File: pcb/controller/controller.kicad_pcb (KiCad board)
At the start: 4 copper layers, 80 x 100 mm, 195 parts, among them J1001 mounting-hole-grounded, J1002 mounting-hole-grounded, J1003 mounting-hole-grounded, J1004 mounting-hole-grounded, J2001 Conn_01x02_Female, J3001 Conn_01x06_Male, J3002 Conn_01x04_Male, J5001 Conn_01x02_Female, J5002 Conn_01x02_Female, J6001 RJ45, J6002 Conn_01x02_Female, J6003 Conn_01x02_Female, J7001 Conn_Coaxial, J7002 Conn_Coaxial, U2001 LMZ14201, U2002 TPS82084, U2003 TPS735, U2004 TPS735, U3001 XC7S25-L1FTGB196, U3002 S25FL127SABN, U3003 74AVC4TD245BQ, U5001 IXDD609D2, U5002 IXDD609D2, U5003 74LVC8T245, U5004 IXDD609D2, U5005 IXDD609D2, U6001 AFBR-1624Z, U6002 AFBR-2624Z, U6003 RFM-0505S, U6004 ISO3086DWR, U6005 ISO7720QDQ1, U6006 ULN2003F12, U7001 MCP6561-OT, U7002 TLV3501AIDBVR, U7003 THS4551RGT, U7004 SG3225, U7005 AD9609

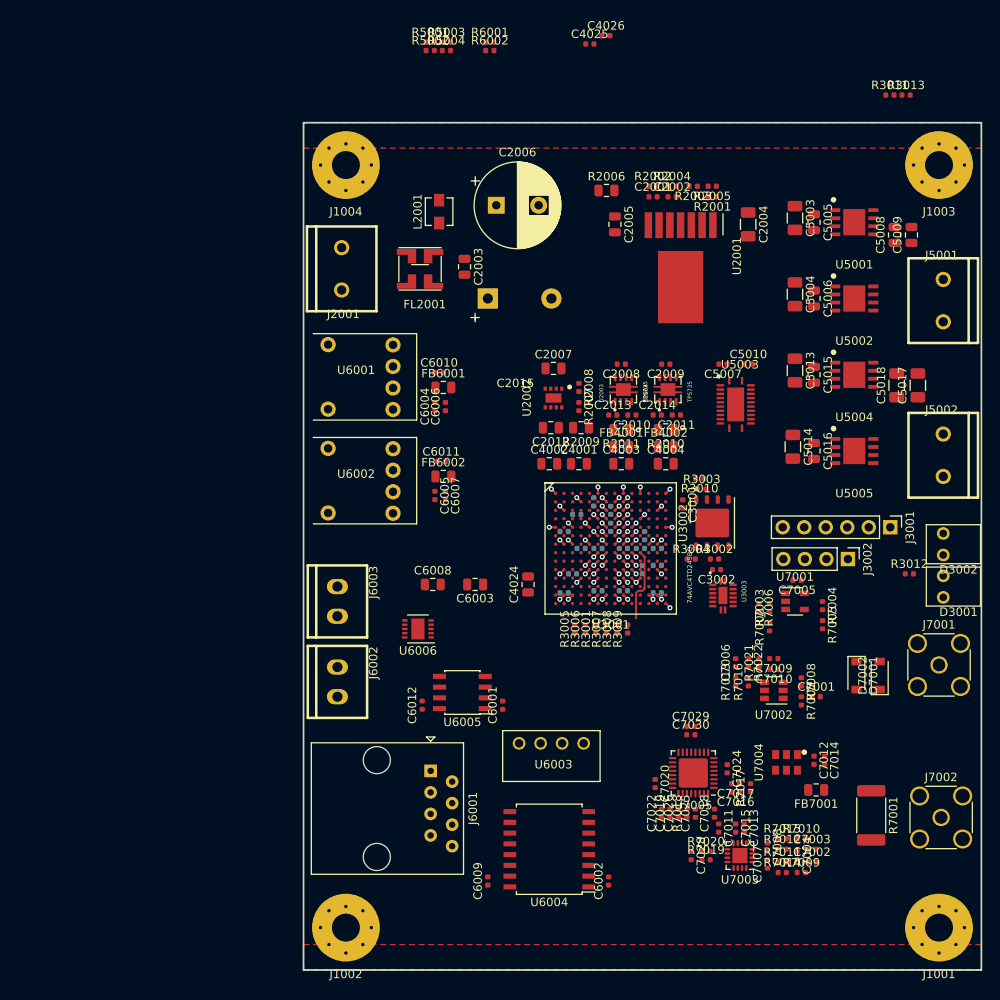
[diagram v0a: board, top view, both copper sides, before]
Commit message: controller PCB routing progress
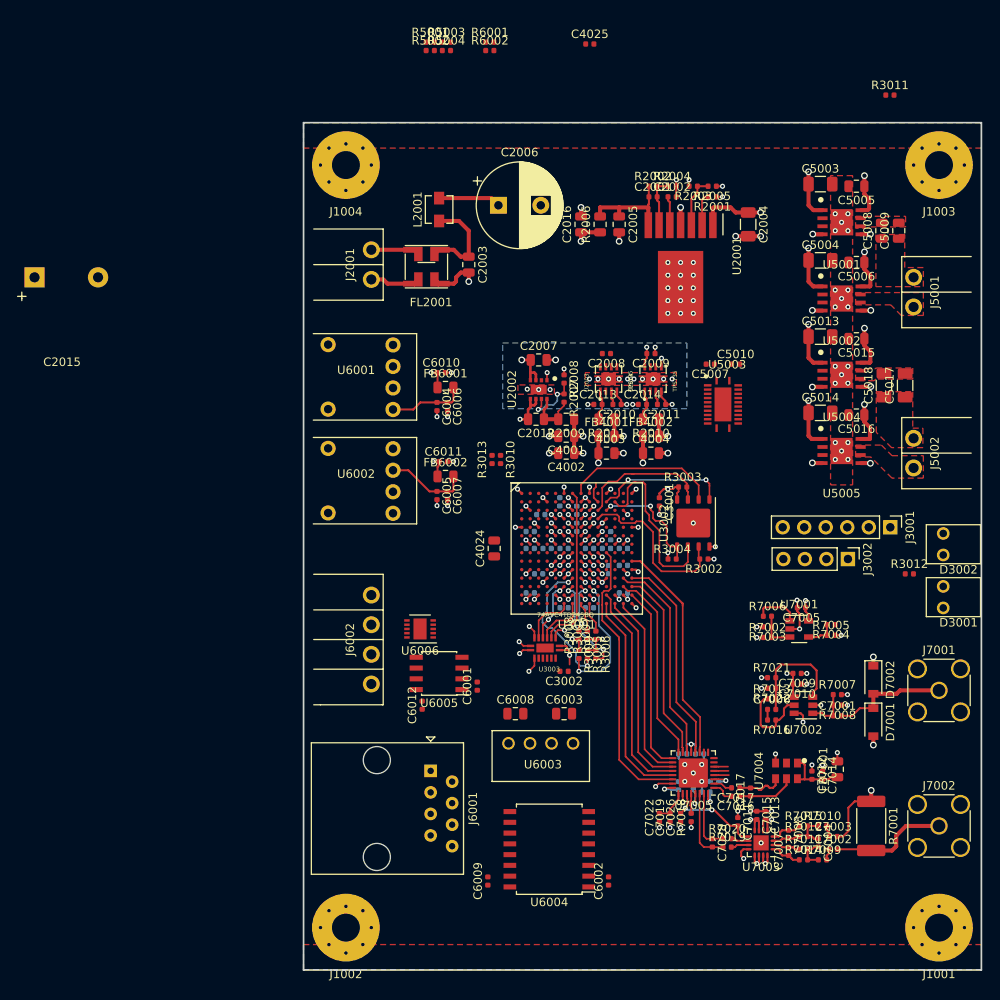
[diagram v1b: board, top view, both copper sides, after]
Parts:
- removed J6003: Conn_01x02_Female, wbraun_smd:terminalBlock-3.5mm-2
- added C2016: 47u, Capacitor_SMD:C_0805_2012Metric, F.Cu at (122.8, 42.0)
- C4026, C7018, C7020, C7024, C7025, C7029, C7030: moved to B.Cu
- J2001, J5001, J5002: footprint wbraun_smd:TerminalBlock-5.0mm-2 -> wbraun_smd:Terminal-block-plug_2x1_3.5mm-pitch
- J6002: value Conn_01x02_Female -> Conn_01x04_Female; footprint wbraun_smd:terminalBlock-3.5mm-2 -> wbraun_smd:Terminal-block-plug_4x1_3.5mm-pitch
- moved R3013 65.1 mm to (112.2, 69.8), turned to 90 degrees
- moved C4026 61.2 mm to (116.8, 80.2)
- moved C2015 53.6 mm to (62.0, 48.2)
- moved R3010 23.6 mm to (113.2, 69.8), turned to 270 degrees
- moved U3003 21.9 mm to (118.5, 92.0), turned to 180 degrees
- moved C3002 21.6 mm to (120.8, 94.8)
- moved C6003 18.5 mm to (120.8, 99.8), turned to 0 degrees
- moved C6008 18.1 mm to (115.0, 99.8)
- moved C7006 6.95 mm to (145.2, 99.2), turned to 0 degrees
- moved C5005 6.56 mm to (155.2, 37.5), turned to 180 degrees
- moved C5006 6.56 mm to (155.2, 46.5), turned to 180 degrees
- moved C5015 6.56 mm to (155.2, 55.5), turned to 180 degrees
- moved C5016 6.56 mm to (155.2, 64.5), turned to 180 degrees
- moved R3009 6.49 mm to (122.5, 92.8), turned to 270 degrees
- moved J6002 6.40 mm to (98.0, 91.0), turned to 90 degrees
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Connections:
- C7016 pad 1: /Analog/CLK_P -> /Analog/CLK_N
- C7017 pad 1: /Analog/CLK_N -> /Analog/CLK_P
- J2001 pad 1: Net-(FL2001-Pad2) -> Net-(FL2001-Pad4)
- J2001 pad 2: Net-(FL2001-Pad4) -> Net-(FL2001-Pad2)
- J6002 pad 1: /Interface/5_ISO -> /Interface/RELAY_B_DRV
- J6002 pad 2: /Interface/RELAY_B_DRV -> /Interface/5_ISO
- R7017 pad 1: /Analog/CLK_P -> /Analog/CLK_N
- R7017 pad 2: /Analog/CLK_N -> /Analog/CLK_P
- U3003 pad 1: +3V3 -> +3V3D
- U3003 pad 16: +3V3 -> +3V3D
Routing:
- net GND: track 33.5 -> 140.3 mm, vias 45 -> 170
- net +24V: track 0.00 -> 61.1 mm, vias 0 -> 10
- net +3V3D: track 7.12 -> 35.4 mm, vias 9 -> 18
- net ADC_D0: track 0.00 -> 26.5 mm
- net ADC_D8: track 0.00 -> 25.7 mm
- net ADC_D9: track 0.00 -> 25.5 mm
- net ADC_DCO: track 8.66 -> 33.6 mm
- net ADC_D1: track 0.00 -> 24.9 mm
- net ADC_D2: track 0.00 -> 24.8 mm
- net ADC_D7: track 0.00 -> 23.5 mm
- net ADC_D4: track 0.00 -> 22.8 mm
- net ADC_D3: track 0.00 -> 22.6 mm
- net ADC_D6: track 0.00 -> 22.2 mm
- net ADC_D5: track 0.00 -> 22.0 mm
- net /FPGA/FLASH_IO1: track 0.00 -> 21.8 mm
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- added copper zone on In2.Cu, net +1V0
- added copper zone on In2.Cu, net +1V8D
- added copper zone on In2.Cu, net +3V3D
- added copper zone on B.Cu, net GND
- added copper zone on F.Cu, net Net-(C5008-Pad1)
- added copper zone on F.Cu, net Net-(C5008-Pad2)
- added copper zone on F.Cu, net Net-(C5017-Pad1)
- added copper zone on F.Cu, net Net-(C5017-Pad2)
- added copper zone on F.Cu, net Net-(J5001-Pad2)
- added copper zone on F.Cu, net Net-(J5002-Pad2)
- removed copper zone on In2.Cu, net +5V

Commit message: routing almost done
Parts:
- C4025: moved to B.Cu
- moved R6001 73.3 mm to (111.5, 93.8), turned to 90 degrees
- moved R6002 72.3 mm to (110.5, 93.8), turned to 90 degrees
- moved C4025 63.8 mm to (115.8, 84.0), turned to 180 degrees
- moved R3011 60.5 mm to (161.5, 87.2)
- moved R5003 50.2 mm to (139.0, 59.0), turned to 90 degrees
- moved R5001 49.5 mm to (136.0, 59.0), turned to 90 degrees
- moved R5002 49.3 mm to (137.0, 59.0), turned to 90 degrees
- moved R5004 48.8 mm to (138.0, 59.0), turned to 90 degrees
- moved J3001 14.4 mm to (145.2, 81.2), turned to 90 degrees
- moved C4024 12.3 mm to (117.5, 69.0), turned to 0 degrees
- moved J3002 10.2 mm to (145.2, 76.8), turned to 90 degrees
- moved C4006 9.22 mm to (122.2, 83.8)
- moved C4023 4.67 mm to (125.0, 75.8), turned to 90 degrees
- moved C5007 3.25 mm to (141.2, 58.5)
- moved C5010 3.25 mm to (144.2, 58.5)
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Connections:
- J3002 pad 1: Net-(J3002-Pad1) -> +3V3D
- J3002 pad 2: Net-(J3002-Pad2) -> /FPGA/DEBUG_TX
- J3002 pad 3: Net-(J3002-Pad3) -> /FPGA/DEBUG_RX
- J3002 pad 4: Net-(J3002-Pad4) -> GND
- J6001 pad 1: Net-(J6001-Pad1) -> /Interface/TX_P
- J6001 pad 2: Net-(J6001-Pad2) -> /Interface/TX_N
- J6001 pad 3: Net-(J6001-Pad3) -> /Interface/RX_P
- J6001 pad 6: Net-(J6001-Pad6) -> /Interface/RX_N
- J6001 pad 7: Net-(J6001-Pad7) -> /Interface/5_ISO
- J6001 pad 8: Net-(J6001-Pad8) -> /Interface/GND_ISO
- U3001 pad B1: Net-(U3001-PadB1) -> FIBER_TX
- U3001 pad B14: Net-(U3001-PadB14) -> GATE_1
- U3001 pad C1: Net-(U3001-PadC1) -> FIBER_RX
- U3001 pad D14: Net-(U3001-PadD14) -> GATE_2
- U3001 pad F14: Net-(U3001-PadF14) -> GATE_3
- U3001 pad G14: Net-(U3001-PadG14) -> /FPGA/DEBUG_TX
- U3001 pad H12: Net-(U3001-PadH12) -> /FPGA/DEBUG_RX
- U3001 pad H13: Net-(U3001-PadH13) -> UVLO
- U3001 pad H14: Net-(U3001-PadH14) -> GATE_4
- U3001 pad J12: Net-(U3001-PadJ12) -> /FPGA/LED2
- U3001 pad J13: Net-(U3001-PadJ13) -> /FPGA/LED1
- U3001 pad K12: Net-(U3001-PadK12) -> ZCS_DETECT
- U3001 pad M1: Net-(U3001-PadM1) -> ADC_MODE
- U3001 pad N1: Net-(U3001-PadN1) -> ADC_SDIO
- U3001 pad P2: Net-(U3001-PadP2) -> ADC_SCLK
- U3001 pad P3: Net-(U3001-PadP3) -> ADC_CSB
- U5003 pad 10: Net-(U5003-Pad10) -> GND
- U5003 pad 15: /Gate Drive/GATE4_5 -> Net-(U5003-Pad15)
- U5003 pad 17: /Gate Drive/GATE3_5 -> Net-(U5003-Pad17)
- U5003 pad 18: Net-(U5003-Pad18) -> /Gate Drive/GATE4_5
- U5003 pad 19: /Gate Drive/GATE2_5 -> /Gate Drive/GATE3_5
- U5003 pad 20: Net-(U5003-Pad20) -> /Gate Drive/GATE2_5
- U5003 pad 4: Net-(U5003-Pad4) -> GATE_2
- U5003 pad 5: GATE_2 -> GATE_3
- U5003 pad 6: Net-(U5003-Pad6) -> GATE_4
- U5003 pad 7: GATE_3 -> GND
- U5003 pad 8: Net-(U5003-Pad8) -> GND
- U5003 pad 9: GATE_4 -> GND
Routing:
- net Net-(J3001-Pad5): track 0.00 -> 49.1 mm, vias 0 -> 1
- net Net-(J3001-Pad4): track 0.00 -> 45.4 mm, vias 0 -> 1
- net ADC_CSB: track 1.76 -> 45.8 mm, vias 0 -> 2
- net /FPGA/LED1: track 0.00 -> 43.7 mm, vias 0 -> 1
- net Net-(J3001-Pad3): track 0.00 -> 41.7 mm, vias 0 -> 1
- net GND: track 140.3 -> 179.2 mm, vias 170 -> 184
- net Net-(J3001-Pad2): track 0.00 -> 37.8 mm, vias 0 -> 1
- net /FPGA/LED2: track 0.00 -> 37.1 mm, vias 0 -> 1
- net ZCS_DETECT: track 9.65 -> 38.4 mm, vias 0 -> 2
- net /FPGA/DEBUG_RX: track 0.00 -> 26.6 mm, vias 0 -> 1
- net GATE_4: track 0.00 -> 25.6 mm, vias 0 -> 2
- net GATE_3: track 0.00 -> 24.8 mm, vias 0 -> 2
- net /FPGA/DEBUG_TX: track 0.00 -> 24.8 mm, vias 0 -> 1
- net /Gate Drive/GATE1_5: track 0.00 -> 24.0 mm
- net GATE_2: track 0.00 -> 21.9 mm, vias 0 -> 2
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
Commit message: controller layout done and schematic reviewed
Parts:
- added R3014: 4.7K, Resistor_SMD:R_0402_1005Metric, F.Cu at (145.8, 84.5)
- added R3015: 4.7K, Resistor_SMD:R_0402_1005Metric, F.Cu at (147.0, 84.5)
- added R6003: 120, Resistor_SMD:R_1206_3216Metric, F.Cu at (111.5, 118.0)
- moved C2015 56.5 mm to (118.5, 48.0)
- moved C6005 3.09 mm to (105.0, 71.0)
- moved C6007 3.09 mm to (106.2, 71.0)
- moved C6011 3.09 mm to (105.8, 67.0)
- moved FB6002 3.09 mm to (106.0, 68.8)
- moved R6001 2.51 mm to (111.2, 96.2), turned to 270 degrees
- moved U6002 1.64 mm to (95.8, 71.0)
- moved C6004 1.25 mm to (105.0, 64.5)
- moved C6006 1.25 mm to (106.2, 64.5)
- moved C6010 1.25 mm to (105.5, 60.5)
- moved FB6001 1.25 mm to (106.0, 62.2)
- moved U6001 1.25 mm to (95.8, 60.8)
- moved C6003 1.06 mm to (120.2, 101.8)
- moved C6008 1.06 mm to (114.5, 101.8)
- moved U6003 1.06 mm to (117.5, 106.8)
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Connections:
- J1001 pad 1: Net-(J1001-Pad1) -> GND
- J1002 pad 1: Net-(J1002-Pad1) -> GND
- J1003 pad 1: Net-(J1003-Pad1) -> GND
- J1004 pad 1: Net-(J1004-Pad1) -> GND
- R2001 pad 1: GND -> +24V
- U3001 pad H2: Net-(U3001-PadH2) -> RELAY_B
- U3001 pad J1: Net-(U3001-PadJ1) -> RELAY_A
- U3001 pad J2: Net-(U3001-PadJ2) -> RS485-D
- U3001 pad L1: Net-(U3001-PadL1) -> RS485-DE
- U3001 pad L2: Net-(U3001-PadL2) -> RS485-RE
- U3001 pad M1: ADC_MODE -> RS485-R
- U3001 pad M2: Net-(U3001-PadM2) -> ADC_MODE
- U6004 pad 11: /Interface/TX_N -> /Interface/TX_P
- U6004 pad 12: /Interface/TX_P -> /Interface/TX_N
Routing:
- net +5V: track 20.0 -> 127.3 mm, vias 6 -> 8
- net RS485-RE: track 0.00 -> 54.0 mm, vias 0 -> 2
- net RS485-R: track 0.00 -> 53.4 mm, vias 0 -> 2
- net RS485-D: track 0.00 -> 53.1 mm, vias 0 -> 2
- net RS485-DE: track 0.00 -> 52.2 mm, vias 0 -> 2
- net ADC_MODE: track 9.51 -> 44.1 mm
- net ADC_SDIO: track 12.0 -> 46.3 mm
- net ADC_SCLK: track 12.3 -> 46.0 mm
- net +24V: track 67.2 -> 100.8 mm, vias 14 -> 16
- net +3V3D: track 45.6 -> 77.5 mm, vias 19 -> 22
- net FIBER_TX: track 0.00 -> 31.5 mm
- net RELAY_A: track 0.00 -> 24.2 mm
- net GND: track 179.2 -> 203.4 mm, vias 184 -> 238
- net RELAY_B: track 0.00 -> 23.6 mm
- net /Interface/RX_P: track 0.00 -> 18.0 mm
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- added copper zone on In2.Cu, net +5V
- added copper zone on In2.Cu, net /Interface/5_ISO
- added copper zone on In1.Cu, net /Interface/GND_ISO
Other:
- board text added: "+24V"
- board text added: "Debug: 3V3 TX RX GND"
- board text added: "Feedback"
- board text added: "GDT 1"
- board text added: "GDT 2"
- board text added: "GND"
- board text added: "JTAG: 3V3 TCK TDI TMS TDO GND"
- board text added: "OCD"
- board text added: "RX"
- board text added: "Relay Drive"
- board text added: "TX"

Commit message: generated gerbers
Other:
- rule pad_to_mask_clearance: 0.051 -> 0.05
- rule solder_mask_min_width: 0.25 -> 0.1
- board text added: "Cute QCW Controller Board wdb@stanford.edu"
- board text added: "Git Hash: 6a7276b4bfc974ebc640f8db9a590584df14782c"
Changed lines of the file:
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@@
   (general
     (thickness 1.6)
-    (drawings 28)
+    (drawings 30)
     (tracks 2063)
     (zones 0)
@@
     (34 B.Paste user)
     (35 F.Paste user hide)
-    (36 B.SilkS user hide)
+    (36 B.SilkS user)
     (37 F.SilkS user)
     (38 B.Mask user)
@@
     (pad_size 1.524 1.524)
     (pad_drill 0.762)
-    (pad_to_mask_clearance 0.051)
-    (solder_mask_min_width 0.25)
+    (pad_to_mask_clearance 0.05)
+    (solder_mask_min_width 0.1)
     (aux_axis_origin 0 0)
     (visible_elements FFF9FF7F)
     (pcbplotparams
-      (layerselection 0x010fc_ffffffff)
+      (layerselection 0x010f0_ffffffff)
       (usegerberextensions false)
       (usegerberattributes false)
@@
       (psnegative false)
       (psa4output false)
-      (plotreference true)
-      (plotvalue true)
+      (plotreference false)
+      (plotvalue false)
       (plotinvisibletext false)
       (padsonsilk false)
@@
       (outputformat 1)
       (mirror false)
-      (drillshape 1)
+      (drillshape 0)
       (scaleselection 1)
-      (outputdirectory ""))
+      (outputdirectory "../../gerbers/controller/"))
   )
   (net 0 "")
@@
     )
   )
+  (gr_text "Cute QCW Controller Board\nwdb@stanford.edu" (at 144.25 122) (layer F.SilkS)
+    (effects (font (size 1.5 1.5) (thickness 0.3)))
+  )
+  (gr_text "Git Hash: 6a7276b4bfc974ebc640f8db9a590584df14782c" (at 142.15 123.2) (layer B.SilkS)
+    (effects (font (size 0.8 0.8) (thickness 0.15)) (justify mirror))
+  )
   (gr_poly (pts (xy 90 130) (xy 90 127) (xy 170 127) (xy 170 130)) (layer B.Mask) (width 0.15))

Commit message: updated schematic component values
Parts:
- C2001: value C -> 22n
- C2002: value C -> 10n
- C2003: value C -> 1u
- C2006: value CP1 -> 470u
- C2015: value CP2 -> 2200u
- C5005, C5006, C5015, C5016: value 0.47u -> 1u
- C5008, C5017: value 1u -> 10u
- C7001: value C -> 0.47u
- C7004: value C -> 43p
- C7006: value C -> DNP
- C7007, C7008, C7028: value C -> 22p
- D7001, D7002: value D -> MBR0540T3G
- FL2001: value EMI_Filter_CommonMode -> DLW5BTM501TQ2
- L2001: value L -> 1u
- R2001: value R -> 100k
- R2002: value R -> 34k
- R2003, R2004, R2007: value R -> 6.49k
- R2005: value R -> 41.2k
- R2008: value R -> 26.1k
- R3011, R3012: value 470 -> 100
- R5001, R5002, R5003, R5004: value 4.7k -> 470
- R6001, R6002: value R -> 470
- R7002, R7003, R7007, R7008, R7021, R7022: value R -> 4.7k
- R7004: value R -> 41.2K
- R7005: value R -> 4.7K
- R7006, R7013, R7016: value R -> DNP
- R7009, R7010, R7014, R7015: value R -> 1k
- R7011, R7012: value R -> 330
- R7017: value R -> 100
- R7018: value R -> 10K
- R7019, R7020: value R -> 33
- U2001: value LMZ14201 -> LMZ14201H
